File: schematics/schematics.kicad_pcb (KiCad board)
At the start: 4 copper layers, 92.5 x 37 mm, 31 parts, among them J1 Conn_SNP59_96_32X3, J2 SWD, J3 Micro_SD_Card_Det1, SW1 RESET, U1 STM32F103VBT6, U2 AMS1117-3.3, Y1 16Mhz

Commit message: Configure ignored files
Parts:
- added C12: 100nF, Capacitor_SMD:C_0603_1608Metric, F.Cu at (77.5, 69.0)
- FB1: value FerriteBead -> 100R @ 100Mhz
- moved C3 14.3 mm to (78.5, 54.8), turned to 180 degrees
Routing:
- net +3.3V: track 255.4 -> 257.4 mm
- net GND: track 43.8 -> 44.7 mm, vias 22 -> 23
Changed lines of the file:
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@@
   )
   (footprint "Capacitor_SMD:C_0603_1608Metric" (layer "F.Cu")
-    (at 77.4 69 90)
+    (at 77.5 69 90)
     (descr "Capacitor SMD 0603 (1608 Metric), square (rectangular) end terminal, IPC_7351 nominal, (Body size source: IPC-SM-782 page 76, https://www.pcb-3d.com/wordpress/wp-content/uploads/ipc-sm-782a_amendment_1_and_2.pdf), generated with kicad-footprint-generator")
     (tags "capacitor")
@@
     (property "ki_keywords" "cap capacitor")
     (attr smd)
-    (fp_text reference "C3" (at 2.2 0 180) (layer "F.Fab")
-        (effects (font (size 1 1) (thickness 0.15)))
-    )
-    (fp_text value "4.7uF" (at 0 1.43 90) (layer "F.Fab")
+    (fp_text reference "C12" (at 0 -1.43 90) (layer "F.Fab")
+        (effects (font (size 1 1) (thickness 0.15)))
+    )
+    (fp_text value "100nF" (at 0 1.43 90) (layer "F.Fab")
         (effects (font (size 1 1) (thickness 0.15)))
     )
@@
       (net 3 "+3.3V") (pintype "passive"))
     (pad "2" smd roundrect (at 0.775 0 90) (size 0.9 0.95) (layers "F.Cu" "F.Paste" "F.Mask") (roundrect_rratio 0.25)
+      (net 2 "GND") (pintype "passive"))
+    (model "${KICAD6_3DMODEL_DIR}/Capacitor_SMD.3dshapes/C_0603_1608Metric.wrl"
+      (offset (xyz 0 0 0))
+      (scale (xyz 1 1 1))
+      (rotate (xyz 0 0 0))
+    )
+  )
+  (footprint "Capacitor_SMD:C_0603_1608Metric" (layer "F.Cu")
+    (at 78.5 54.75 180)
+    (descr "Capacitor SMD 0603 (1608 Metric), square (rectangular) end terminal, IPC_7351 nominal, (Body size source: IPC-SM-782 page 76, https://www.pcb-3d.com/wordpress/wp-content/uploads/ipc-sm-782a_amendment_1_and_2.pdf), generated with kicad-footprint-generator")
+    (tags "capacitor")
+    (property "Sheetfile" "schematics.kicad_sch")
+    (property "Sheetname" "")
+    (property "ki_description" "Unpolarized capacitor")
+    (property "ki_keywords" "cap capacitor")
+    (attr smd)
+    (fp_text reference "C3" (at 2.2 0 90) (layer "F.Fab")
+        (effects (font (size 1 1) (thickness 0.15)))
+    )
+    (fp_text value "4.7uF" (at 0 1.43) (layer "F.Fab")
+        (effects (font (size 1 1) (thickness 0.15)))
+    )
+    (fp_text user "${REFERENCE}" (at 0 0) (layer "F.Fab")
+        (effects (font (size 0.4 0.4) (thickness 0.06)))
+    )
+    (fp_line (start -0.14058 -0.51) (end 0.14058 -0.51)
+      (stroke (width 0.12) (type solid)) (layer "F.SilkS"))
+    (fp_line (start -0.14058 0.51) (end 0.14058 0.51)
+      (stroke (width 0.12) (type solid)) (layer "F.SilkS"))
+    (fp_line (start -1.48 -0.73) (end 1.48 -0.73)
+      (stroke (width 0.05) (type solid)) (layer "F.CrtYd"))
+    (fp_line (start -1.48 0.73) (end -1.48 -0.73)
+      (stroke (width 0.05) (type solid)) (layer "F.CrtYd"))
+    (fp_line (start 1.48 -0.73) (end 1.48 0.73)
+      (stroke (width 0.05) (type solid)) (layer "F.CrtYd"))
+    (fp_line (start 1.48 0.73) (end -1.48 0.73)
+      (stroke (width 0.05) (type solid)) (layer "F.CrtYd"))
+    (fp_line (start -0.8 -0.4) (end 0.8 -0.4)
+      (stroke (width 0.1) (type solid)) (layer "F.Fab"))
+    (fp_line (start -0.8 0.4) (end -0.8 -0.4)
+      (stroke (width 0.1) (type solid)) (layer "F.Fab"))
+    (fp_line (start 0.8 -0.4) (end 0.8 0.4)
+      (stroke (width 0.1) (type solid)) (layer "F.Fab"))
+    (fp_line (start 0.8 0.4) (end -0.8 0.4)
+      (stroke (width 0.1) (type solid)) (layer "F.Fab"))
+    (pad "1" smd roundrect (at -0.775 0 180) (size 0.9 0.95) (layers "F.Cu" "F.Paste" "F.Mask") (roundrect_rratio 0.25)
+      (net 3 "+3.3V") (pintype "passive"))
+    (pad "2" smd roundrect (at 0.775 0 180) (size 0.9 0.95) (layers "F.Cu" "F.Paste" "F.Mask") (roundrect_rratio 0.25)
       (net 2 "GND") (pintype "passive"))
     (model "${KICAD6_3DMODEL_DIR}/Capacitor_SMD.3dshapes/C_0603_1608Metric.wrl"
@@
         (effects (font (size 1 1) (thickness 0.15)))
     )
-    (fp_text value "FerriteBead" (at 0 1.43 90) (layer "F.Fab")
+    (fp_text value "100R @ 100Mhz" (at 0 1.43 90) (layer "F.Fab")
         (effects (font (size 1 1) (thickness 0.15)))
     )
@@
   (segment (start 82.525 54.75) (end 82.5 54.775) (width 0.3) (layer "F.Cu") (net 2))
   (segment (start 80.325 63.75) (end 78.675 63.75) (width 0.3) (layer "F.Cu") (net 2))
+  (segment (start 77.725 53.775) (end 77.725 54.75) (width 0.5) (layer "F.Cu") (net 2))
   (segment (start 82.5 54.775) (end 82.5 57.575) (width 0.3) (layer "F.Cu") (net 2))
   (segment (start 77.425 68.25) (end 77.4 68.225) (width 0.3) (layer "F.Cu") (net 2))
@@
   (segment (start 80.85 75.75) (end 81.925 75.75) (width 0.3) (layer "F.Cu") (net 2))
   (segment (start 77.4 61.4) (end 77.4 62.475) (width 0.3) (layer "F.Cu") (net 2))
-  (segment (start 82.525 53.775) (end 82.525 54.75) (width 0.3) (layer "F.Cu") (net 2))
-  (segment (start 84.175 54.75) (end 84.175 53.75) (width 0.3) (layer "F.Cu") (net 2))
+  (segment (start 82.525 53.775) (end 82.525 54.75) (width 0.5) (layer "F.Cu") (net 2))
+  (segment (start 84.175 54.75) (end 84.175 53.75) (width 0.5) (layer "F.Cu") (net 2))
   (segment (start 132.5 61.7125) (end 132.5 62.75) (width 0.5) (layer "F.Cu") (net 2))
   (segment (start 95.675 59.75) (end 98.475 59.75) (width 0.3) (layer "F.Cu") (net 2))
@@
   (via (at 48.53 62.25) (size 0.7) (drill 0.3) (layers "F.Cu" "B.Cu") (net 2))
   (via (at 117.3 62.2) (size 0.7) (drill 0.3) (layers "F.Cu" "B.Cu") (net 2))
+  (via (at 77.725 53.775) (size 0.7) (drill 0.3) (layers "F.Cu" "B.Cu") (net 2))
   (via (at 82.525 53.775) (size 0.7) (drill 0.3) (layers "F.Cu" "B.Cu") (net 2))
   (via (at 48 45) (size 0.7) (drill 0.3) (layers "F.Cu" "B.Cu") (net 2))
@@
   (segment (start 108.75 61.5) (end 110.25 60) (width 0.5) (layer "F.Cu") (net 3))
   (segment (start 77.925 69.25) (end 77.4 69.775) (width 0.3) (layer "F.Cu") (net 3))
-  (segment (start 75.5 53.75) (end 76.25 53) (width 0.5) (layer "F.Cu") (net 3))
   (segment (start 82 57.5) (end 82 57.575) (width 0.3) (layer "F.Cu") (net 3))
   (segment (start 122.5 53.5) (end 121.95 52.95) (width 0.5) (layer "F.Cu") (net 3))
@@
   (segment (start 63.5 71.2125) (end 65.5 71.2125) (width 0.5) (layer "F.Cu") (net 3))
   (segment (start 127.500001 65.962499) (end 127.4625 66) (width 0.5) (layer "F.Cu") (net 3))
+  (segment (start 76.275 64.275) (end 75.5 63.5) (width 0.5) (layer "F.Cu") (net 3))
   (segment (start 120.5 76.25) (end 120.5 63.75) (width 0.5) (layer "F.Cu") (net 3))
   (segment (start 96.675 58.25) (end 95.675 59.25) (width 0.3) (layer "F.Cu") (net 3))
@@
   (segment (start 122 55.75) (end 122.5 56.25) (width 0.5) (layer "F.Cu") (net 3))
   (segment (start 83.5 75.8) (end 83.5 76.75) (width 0.5) (layer "F.Cu") (net 3))
-  (segment (start 77.4 64.025) (end 76.025 64.025) (width 0.5) (layer "F.Cu") (net 3))
   (segment (start 83 72.925) (end 83 75.275) (width 0.3) (layer "F.Cu") (net 3))
   (segment (start 75.5 70.5) (end 75.5 76.25) (width 0.5) (layer "F.Cu") (net 3))
+  (segment (start 79.275 54.75) (end 80.975 54.75) (width 0.5) (layer "F.Cu") (net 3))
   (segment (start 76.25 52.95) (end 55.25 52.95) (width 0.5) (layer "F.Cu") (net 3))
   (segment (start 76.25 53) (end 76.25 52.95) (width 0.3) (layer "F.Cu") (net 3))
@@
   (segment (start 120.5 58.75) (end 121.025 58.225) (width 0.5) (layer "F.Cu") (net 3))
   (segment (start 107 64.33) (end 107.92 64.33) (width 0.5) (layer "F.Cu") (net 3))
+  (segment (start 77.5 64.275) (end 76.275 64.275) (width 0.5) (layer "F.Cu") (net 3))
   (segment (start 67.5375 71.25) (end 67.5 71.2125) (width 0.5) (layer "F.Cu") (net 3))
   (segment (start 54.655 53.545) (end 55.25 52.95) (width 0.5) (layer "F.Cu") (net 3))
@@
   (segment (start 94.5 75.775) (end 94.475 75.75) (width 0.5) (layer "F.Cu") (net 3))
   (segment (start 121.95 52.95) (end 81.25 52.95) (width 0.5) (layer "F.Cu") (net 3))
-  (segment (start 76.025 64.025) (end 75.5 63.5) (width 0.5) (layer "F.Cu") (net 3))
+  (segment (start 75.5 63.5) (end 75.5 53.75) (width 0.5) (layer "F.Cu") (net 3))
   (segment (start 119 55.75) (end 122 55.75) (width 0.5) (layer "F.Cu") (net 3))
   (segment (start 76.225 69.775) (end 75.5 70.5) (width 0.5) (layer "F.Cu") (net 3))
+  (segment (start 75.5 53.75) (end 76.25 53) (width 0.5) (layer "F.Cu") (net 3))
   (segment (start 76.25 77) (end 119.75 77) (width 0.5) (layer "F.Cu") (net 3))
   (segment (start 80.975 56.475) (end 82 57.5) (width 0.3) (layer "F.Cu") (net 3))
@@
   (segment (start 120.5 63.75) (end 120.5 58.75) (width 0.5) (layer "F.Cu") (net 3))
   (segment (start 50.73 53.52) (end 50.73 61) (width 0.5) (layer "F.Cu") (net 3))
-  (segment (start 75.5 63.5) (end 75.5 53.75) (width 0.5) (layer "F.Cu") (net 3))
   (segment (start 110.25 60) (end 120.5 60) (width 0.5) (layer "F.Cu") (net 3))
   (segment (start 122.5 56.25) (end 122.5 58.225) (width 0.5) (layer "F.Cu") (net 3))

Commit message: Update the board schematics
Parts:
- removed FB1: 100R @ 100Mhz, Inductor_SMD:L_0603_1608Metric
- added J4: POWER, Connector_JST:JST_EH_B2B-EH-A_1x02_P2.50mm_Vertical, F.Cu at (107.3, 114.2)
- added R10: 10k, Resistor_SMD:R_0603_1608Metric, F.Cu at (171.8, 109.2)
- added R11: 10k, Resistor_SMD:R_0603_1608Metric, F.Cu at (179.0, 114.2)
- added R9: 10k, Resistor_SMD:R_0603_1608Metric, F.Cu at (169.8, 109.2)
- C1: value 22uF -> 4.7uF
- C10, C9: value 10pF -> 100nF
- C3: value 4.7uF -> 100nF
- C4, C5: value 100nF -> 10pF
- C7: value 100nF -> 22uF
- J1: value Conn_SNP59_96_32X3 -> 2K; footprint Custom:SNP59-96 -> Custom:RPP_48G2_3T3_Male
- J2: footprint Connector_PinHeader_2.54mm:PinHeader_1x04_P2.54mm_Vertical -> Connector_PinHeader_1.27mm:PinHeader_2x07_P1.27mm_Vertical_SMD
- J3: value Micro_SD_Card_Det1 -> Micro SD Card
- R2: value 1.5k -> 10R
- R3, R4: value 10k -> 1.5k
- R5: value 10R -> 1.5k
- R7, R8: value 1.5k -> 10k
- SW1: footprint Custom:SW_Push_SMD_4x4x1.5 -> Button_Switch_THT:SW_PUSH_6mm_H4.3mm
- moved J3 147.2 mm to (192.5, 114.3), turned to 90 degrees
- moved R7 107.8 mm to (167.8, 109.2), turned to 90 degrees
- moved C12 104.3 mm to (173.8, 109.2)
- moved R8 104.0 mm to (165.8, 109.2)
- moved C10 99.8 mm to (160.7, 107.4), turned to -90 degrees
- moved R4 91.5 mm to (122.8, 118.5)
- moved C9 81.2 mm to (149.0, 95.8), turned to 0 degrees
- moved C4 80.8 mm to (128.8, 120.5), turned to 180 degrees
- moved J2 80.8 mm to (169.8, 115.2), turned to 90 degrees
- moved C11 79.4 mm to (148.8, 119.7)
- moved C6 79.3 mm to (139.2, 113.2), turned to 135 degrees
- moved C3 79.0 mm to (137.3, 107.5), turned to 90 degrees
- moved Y1 76.6 mm to (128.8, 117.0)
- moved D2 76.4 mm to (122.8, 120.2), turned to 0 degrees
- moved C8 74.4 mm to (143.9, 117.9), turned to 135 degrees
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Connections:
- C1 pad 1: /PWR -> +3.3V
- C10 pad 1: OSC_IN -> +3.3V
- C12 pad 1: +3.3V -> NRST
- C2 pad 1: +3.3V -> /VBUS
- C4 pad 1: +3.3V -> Net-(C4-Pad1)
- C5 pad 1: NRST -> OSC_IN
- C9 pad 1: OSC_OUT -> +3.3V
- J1 pad 1: GND -> External_Set_Output
- J1 pad 10: unconnected-(J1-10C-Pad10) -> Data_Bus_Input_02
- J1 pad 11: unconnected-(J1-11C-Pad11) -> Data_Bus_Input_00
- J1 pad 12: unconnected-(J1-12C-Pad12) -> Data_Bus_Input_Control_1
- J1 pad 13: unconnected-(J1-13C-Pad13) -> Data_Bus_Input_08
- J1 pad 14: unconnected-(J1-14C-Pad14) -> Data_Transfer_Short_Input
- J1 pad 15: unconnected-(J1-15C-Pad15) -> Data_Bus_Input_09
- J1 pad 16: unconnected-(J1-16C-Pad16) -> Data_Bus_Input_11
- J1 pad 17: unconnected-(J1-17C-Pad17) -> Data_Bus_Input_12
- J1 pad 18: unconnected-(J1-18C-Pad18) -> Data_Bus_Input_10
- J1 pad 19: unconnected-(J1-19C-Pad19) -> Data_Bus_Input_Control_0
- J1 pad 20: unconnected-(J1-20C-Pad20) -> Data_Bus_Input_14
- J1 pad 21: unconnected-(J1-21C-Pad21) -> Data_Bus_Input_15
- J1 pad 22: unconnected-(J1-22C-Pad22) -> Data_Bus_Input_13
- J1 pad 23: unconnected-(J1-23C-Pad23) -> Data_Transfer_Completed_Output
- J1 pad 24: unconnected-(J1-24C-Pad24) -> Data_Bus_Output_Control_State
- J1 pad 25: unconnected-(J1-25C-Pad25) -> Internal_Error_Output
- J1 pad 26: unconnected-(J1-26C-Pad26) -> Data_Bus_Output_00
- J1 pad 27: unconnected-(J1-27C-Pad27) -> Data_Bus_Output_Control_0
- J1 pad 28: unconnected-(J1-28C-Pad28) -> Data_Bus_Output_01
- J1 pad 29: unconnected-(J1-29C-Pad29) -> Data_Bus_Output_Control_1
- J1 pad 3: unconnected-(J1-3C-Pad3) -> Data_Bus_Input_05
- J1 pad 30: unconnected-(J1-30C-Pad30) -> Data_Bus_Output_02
- J1 pad 31: unconnected-(J1-31C-Pad31) -> Data_Bus_Output_04
- J1 pad 32: VBUS -> Data_Bus_Output_03
- J1 pad 33: GND -> Data_Bus_Output_06
- J1 pad 34: unconnected-(J1-2B-Pad34) -> Data_Bus_Output_05
- J1 pad 35: unconnected-(J1-3B-Pad35) -> Data_Bus_Output_07
- J1 pad 36: unconnected-(J1-4B-Pad36) -> Data_Bus_Output_09
- J1 pad 37: unconnected-(J1-5B-Pad37) -> Data_Bus_Output_10
- J1 pad 38: unconnected-(J1-6B-Pad38) -> Data_Bus_Output_08
- J1 pad 39: unconnected-(J1-7B-Pad39) -> Data_Bus_Output_12
- J1 pad 4: unconnected-(J1-4C-Pad4) -> Data_Bus_Input_07
- J1 pad 40: unconnected-(J1-8B-Pad40) -> Data_Bus_Output_13
- J1 pad 41: unconnected-(J1-9B-Pad41) -> Data_Bus_Output_15
- J1 pad 42: unconnected-(J1-10B-Pad42) -> Ready_Output
- J1 pad 43: unconnected-(J1-11B-Pad43) -> Data_Bus_Output_14
- J1 pad 44: unconnected-(J1-12B-Pad44) -> Data_Bus_Output_11
- J1 pad 45: unconnected-(J1-13B-Pad45) -> Data_Transfer_Long_Input
- J1 pad 46: unconnected-(J1-14B-Pad46) -> Data_Transfer_Completed_Input
- J1 pad 47: unconnected-(J1-15B-Pad47) -> External_Reset_Output
- J1 pad 5: unconnected-(J1-5C-Pad5) -> Data_Bus_Input_04
- J1 pad 6: unconnected-(J1-6C-Pad6) -> Data_Bus_Input_06
- J1 pad 7: unconnected-(J1-7C-Pad7) -> Data_Bus_Input_01
- J1 pad 8: unconnected-(J1-8C-Pad8) -> Data_Bus_Input_03
- J1 pad 9: unconnected-(J1-9C-Pad9) -> Reset_Input
- J2 pad 1: +3.3V -> unconnected-(J2-NC-Pad1)
- J2 pad 2: SWDIO -> unconnected-(J2-NC-Pad2)
- J2 pad 3: SWCLK -> +3.3V
- J2 pad 4: GND -> SWDIO
- R2 pad 1: /LED -> Net-(C4-Pad1)
- R2 pad 2: GND -> OSC_OUT
- R3 pad 1: +3.3V -> /LED
- R3 pad 2: NRST -> GND
- R4 pad 1: SPI1_CS -> Net-(D2-K)
- R4 pad 2: +3.3V -> SDMMC_ABSENT_LED
- R5 pad 1: OSC_OUT -> Net-(D3-K)
- R5 pad 2: OSC_OUT -> SDMMC_ERR_LED
- R6 pad 1: Net-(D2-K) -> Net-(D4-K)
- R6 pad 2: SDMMC_ABSENT_LED -> BUS_ERR_LED
- R7 pad 1: Net-(D3-K) -> SWCLK
- R7 pad 2: SDMMC_ERR_LED -> GND
- R8 pad 1: Net-(D4-K) -> +3.3V
- R8 pad 2: BUS_ERR_LED -> SWDIO
- U1 pad 1: unconnected-(U1-PE2-Pad1) -> Data_Bus_Input_04
- U1 pad 2: unconnected-(U1-PE3-Pad2) -> Data_Bus_Input_06
- U1 pad 3: unconnected-(U1-PE4-Pad3) -> Data_Bus_Input_05
- U1 pad 4: unconnected-(U1-PE5-Pad4) -> Data_Bus_Input_07
- U1 pad 48: unconnected-(U1-PB11-Pad48) -> Data_Transfer_Short_Input
- U1 pad 5: unconnected-(U1-PE6-Pad5) -> External_Set_Output
- U1 pad 51: unconnected-(U1-PB12-Pad51) -> External_Reset_Output
- U1 pad 52: unconnected-(U1-PB13-Pad52) -> Data_Transfer_Long_Input
- U1 pad 53: unconnected-(U1-PB14-Pad53) -> Data_Transfer_Completed_Input
- U1 pad 54: unconnected-(U1-PB15-Pad54) -> Data_Bus_Output_14
- U1 pad 55: unconnected-(U1-PD8-Pad55) -> Data_Bus_Output_11
- U1 pad 56: unconnected-(U1-PD9-Pad56) -> Data_Bus_Output_15
- U1 pad 57: unconnected-(U1-PD10-Pad57) -> Ready_Output
- U1 pad 58: unconnected-(U1-PD11-Pad58) -> Data_Bus_Output_12
- U1 pad 59: unconnected-(U1-PD12-Pad59) -> Data_Bus_Output_13
- U1 pad 60: unconnected-(U1-PD13-Pad60) -> Data_Bus_Output_10
- U1 pad 61: unconnected-(U1-PD14-Pad61) -> Data_Bus_Output_08
- U1 pad 62: unconnected-(U1-PD15-Pad62) -> Data_Bus_Output_07
- U1 pad 63: unconnected-(U1-PC6-Pad63) -> Data_Bus_Output_09
- U1 pad 64: unconnected-(U1-PC7-Pad64) -> Data_Bus_Output_06
- U1 pad 65: unconnected-(U1-PC8-Pad65) -> Data_Bus_Output_05
- U1 pad 66: unconnected-(U1-PC9-Pad66) -> Data_Bus_Output_04
- U1 pad 67: unconnected-(U1-PA8-Pad67) -> Data_Bus_Output_03
- U1 pad 68: unconnected-(U1-PA9-Pad68) -> Data_Bus_Output_Control_1
- U1 pad 69: unconnected-(U1-PA10-Pad69) -> Data_Bus_Output_02
- U1 pad 70: unconnected-(U1-PA11-Pad70) -> Data_Bus_Output_Control_0
- U1 pad 71: unconnected-(U1-PA12-Pad71) -> Data_Bus_Output_01
- U1 pad 77: unconnected-(U1-PA15-Pad77) -> Internal_Error_Output
- U1 pad 78: unconnected-(U1-PC10-Pad78) -> Data_Bus_Output_00
- U1 pad 79: unconnected-(U1-PC11-Pad79) -> Data_Transfer_Completed_Output
- U1 pad 80: unconnected-(U1-PC12-Pad80) -> Data_Bus_Output_Control_State
- U1 pad 81: unconnected-(U1-PD0-Pad81) -> Data_Bus_Input_15
- U1 pad 82: unconnected-(U1-PD1-Pad82) -> Data_Bus_Input_13
- U1 pad 83: unconnected-(U1-PD2-Pad83) -> Data_Bus_Input_Control_0
- U1 pad 84: unconnected-(U1-PD3-Pad84) -> Data_Bus_Input_14
- U1 pad 85: unconnected-(U1-PD4-Pad85) -> Data_Bus_Input_12
- U1 pad 86: unconnected-(U1-PD5-Pad86) -> Data_Bus_Input_10
- U1 pad 87: unconnected-(U1-PD6-Pad87) -> Data_Bus_Input_09
- U1 pad 88: unconnected-(U1-PD7-Pad88) -> Data_Bus_Input_11
- U1 pad 89: unconnected-(U1-PB3-Pad89) -> SWO
- U1 pad 90: unconnected-(U1-PB4-Pad90) -> Data_Bus_Input_08
- U1 pad 92: unconnected-(U1-PB6-Pad92) -> Data_Bus_Input_00
- U1 pad 93: unconnected-(U1-PB7-Pad93) -> Data_Bus_Input_Control_1
- U1 pad 95: unconnected-(U1-PB8-Pad95) -> Reset_Input
- U1 pad 96: unconnected-(U1-PB9-Pad96) -> Data_Bus_Input_02
- U1 pad 97: unconnected-(U1-PE0-Pad97) -> Data_Bus_Input_01
- U1 pad 98: unconnected-(U1-PE1-Pad98) -> Data_Bus_Input_03
- U2 pad 3: /PWR -> /VBUS
- Y1 pad 3: OSC_OUT -> Net-(C4-Pad1)
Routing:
- net +3.3V: track 257.4 -> 141.9 mm, vias 1 -> 2
- net External_Set_Output: track 0.00 -> 57.2 mm, vias 0 -> 2
- net Data_Bus_Input_07: track 0.00 -> 52.7 mm, vias 0 -> 1
- net Data_Bus_Input_06: track 0.00 -> 51.3 mm, vias 0 -> 1
- net Data_Bus_Input_04: track 0.00 -> 49.0 mm, vias 0 -> 2
- net Data_Bus_Input_05: track 0.00 -> 46.4 mm, vias 0 -> 2
- net External_Reset_Output: track 0.00 -> 46.2 mm
- net Data_Transfer_Completed_Input: track 0.00 -> 46.2 mm, vias 0 -> 1
- net Data_Transfer_Short_Input: track 0.00 -> 43.5 mm, vias 0 -> 1
- net Data_Bus_Output_11: track 0.00 -> 43.0 mm, vias 0 -> 1
- net Data_Transfer_Long_Input: track 0.00 -> 42.6 mm
- net Ready_Output: track 0.00 -> 39.7 mm, vias 0 -> 1
- net Data_Bus_Output_14: track 0.00 -> 39.4 mm
- net Data_Bus_Input_03: track 0.00 -> 38.2 mm, vias 0 -> 1
- net SWO: track 0.00 -> 36.4 mm, vias 0 -> 2
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- added copper zone on B.Cu, net /VBUS
- added copper zone on F.Cu, net /VBUS
- removed copper zone on F.Cu, net /PWR
- removed copper zone on F.Cu, net GND
- removed copper zone on F.Cu, net VBUS
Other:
- board size 92.5 x 37 mm -> 96 x 35 mm
- board text added: "+5V"
- board text added: "Supports SD and SDHC cards"
- board text removed: "3.3V"
- board text removed: "CLK"
- board text removed: "Developed by Artem Korobko https://github.com/artemkorobko"
- board text removed: "IO"

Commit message: Add QR code to the board
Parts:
- added GitHub: LOGO, LOGO, B.Cu at (185.0, 101.0)

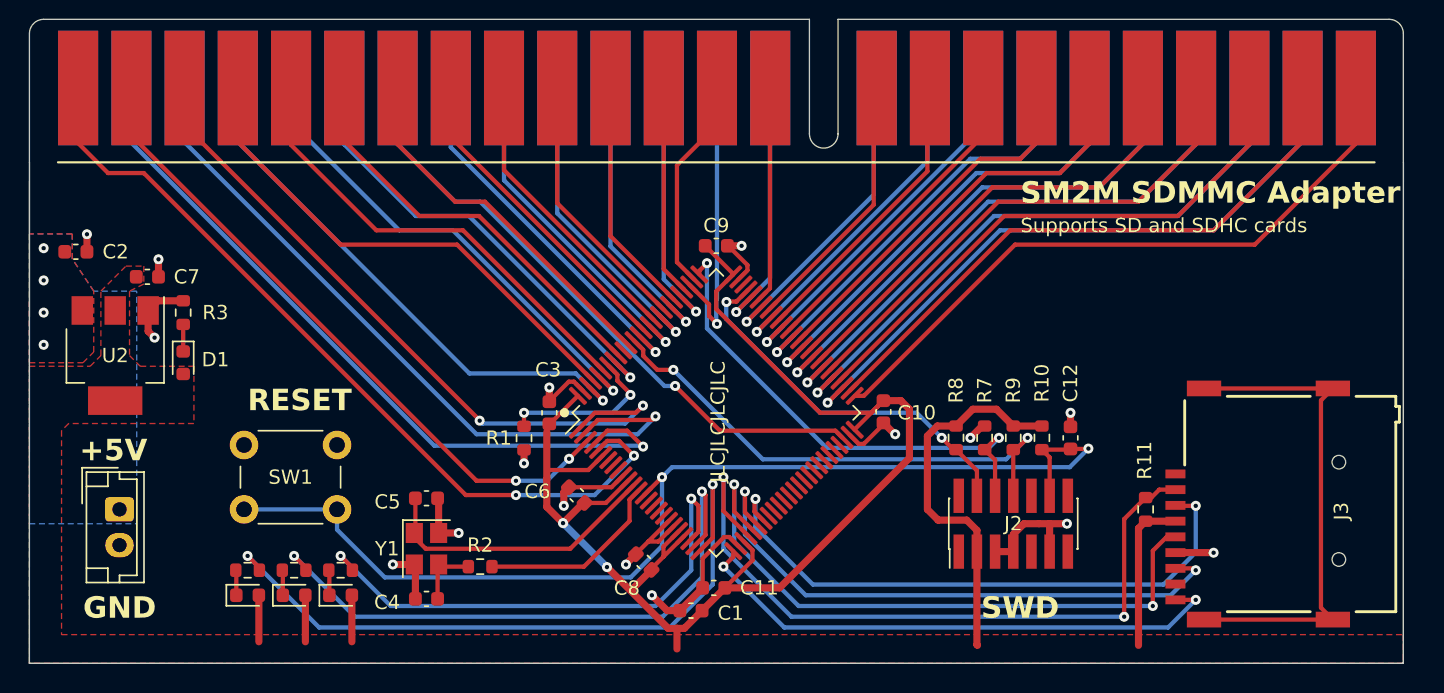
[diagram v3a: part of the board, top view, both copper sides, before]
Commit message: Re-route data buses and add heap allocator
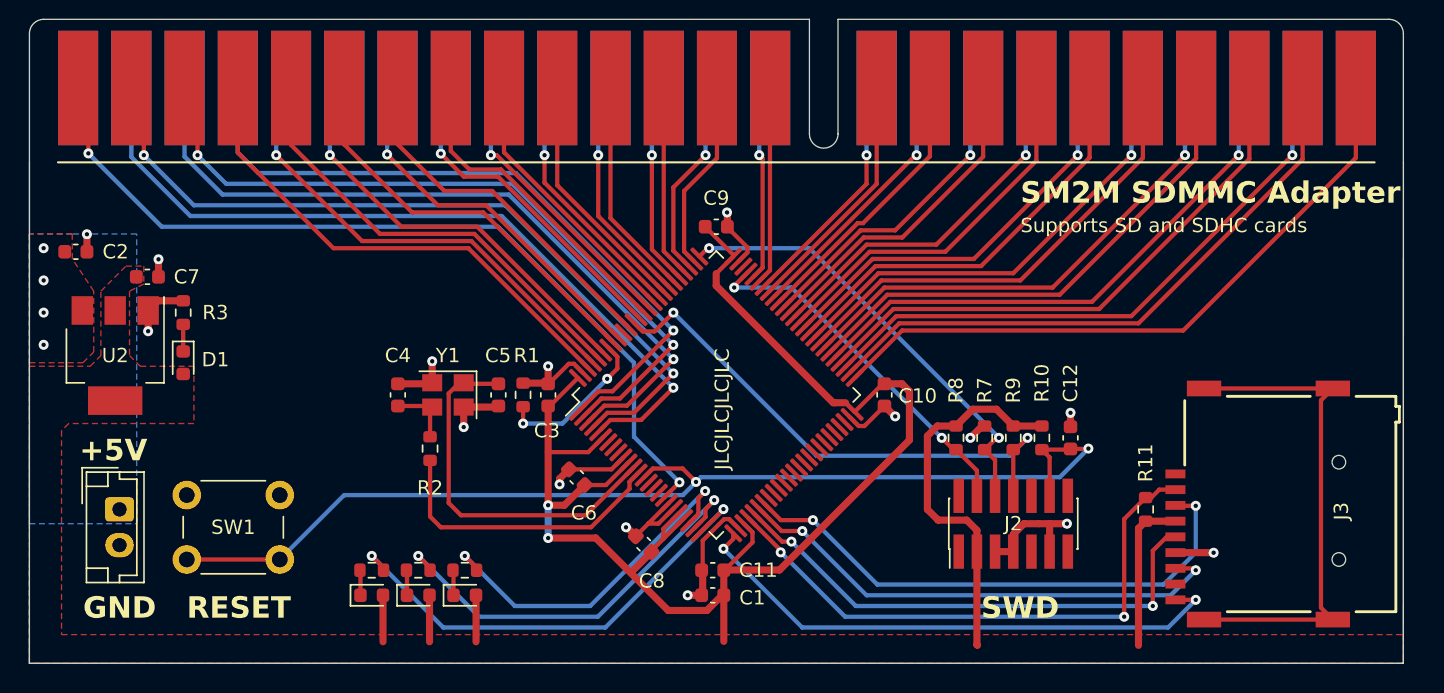
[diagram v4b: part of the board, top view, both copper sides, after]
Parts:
- removed GitHub: LOGO, LOGO
- moved C4 14.4 mm to (126.8, 106.2), turned to 90 degrees
- moved Y1 10.9 mm to (130.2, 106.2), turned to 180 degrees
- moved R2 8.96 mm to (129.0, 110.0), turned to -90 degrees
- moved C5 8.80 mm to (133.8, 106.2), turned to -90 degrees
- moved D2 8.68 mm to (131.4, 120.2)
- moved D3 8.68 mm to (128.2, 120.2)
- moved R4 8.68 mm to (131.4, 118.5)
- moved R5 8.68 mm to (128.2, 118.5)
- moved D4 8.67 mm to (124.9, 120.2)
- moved R6 8.67 mm to (124.9, 118.5)
- moved SW1 5.32 mm to (118.5, 117.8)
- moved R1 3.02 mm to (135.5, 106.2), turned to -90 degrees
- moved C1 1.86 mm to (148.8, 120.2)
- moved C9 1.33 mm to (149.0, 94.5)
- moved C3 1.25 mm to (137.2, 106.2)
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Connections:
- net SDMMC_ABSENT_LED renamed SDMMC_DETACHED_LED
- U1 pad 1: Data_Bus_Input_04 -> Data_Bus_Input_03
- U1 pad 18: unconnected-(U1-PC3-Pad18) -> External_Set_Output
- U1 pad 2: Data_Bus_Input_06 -> Data_Bus_Input_04
- U1 pad 3: Data_Bus_Input_05 -> Data_Bus_Input_06
- U1 pad 4: Data_Bus_Input_07 -> Data_Bus_Input_05
- U1 pad 48: Data_Transfer_Short_Input -> unconnected-(U1-PB11-Pad48)
- U1 pad 5: External_Set_Output -> Data_Bus_Input_07
- U1 pad 92: Data_Bus_Input_00 -> Data_Transfer_Short_Input
- U1 pad 93: Data_Bus_Input_Control_1 -> Data_Bus_Input_00
- U1 pad 95: Reset_Input -> Data_Bus_Input_Control_1
- U1 pad 96: Data_Bus_Input_02 -> Reset_Input
- U1 pad 97: Data_Bus_Input_01 -> Data_Bus_Input_02
- U1 pad 98: Data_Bus_Input_03 -> Data_Bus_Input_01
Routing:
- net Data_Transfer_Short_Input: track 43.5 -> 26.4 mm
- net BUS_ERR_LED: track 49.2 -> 33.8 mm
- net SDMMC_ERR_LED: track 43.0 -> 29.7 mm
- net SDMMC_DETACHED_LED: track 36.8 -> 25.6 mm
- net Data_Bus_Input_03: track 38.2 -> 49.1 mm
- net SPI1_CS: track 51.1 -> 40.4 mm
- net Data_Bus_Input_05: track 46.4 -> 55.5 mm
- net SPI1_SCK: track 44.8 -> 36.4 mm
- net OSC_OUT: track 13.3 -> 20.7 mm
- net SPI1_MISO: track 41.3 -> 35.3 mm
- net OSC_IN: track 20.2 -> 26.1 mm
- net Data_Bus_Output_00: track 20.1 -> 14.2 mm
- net Data_Bus_Output_02: track 21.8 -> 17.2 mm
- net Data_Bus_Output_03: track 23.7 -> 19.2 mm
- net Data_Bus_Output_01: track 18.3 -> 13.9 mm
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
